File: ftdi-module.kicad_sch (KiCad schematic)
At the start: 56 parts, among them U1 USB4145-03-0070-c_REVA2, U2 ISO1641, U3 NCP163ASN330T1G, U5 FT4232H-56Q, Y1 KX-7_12,MHz

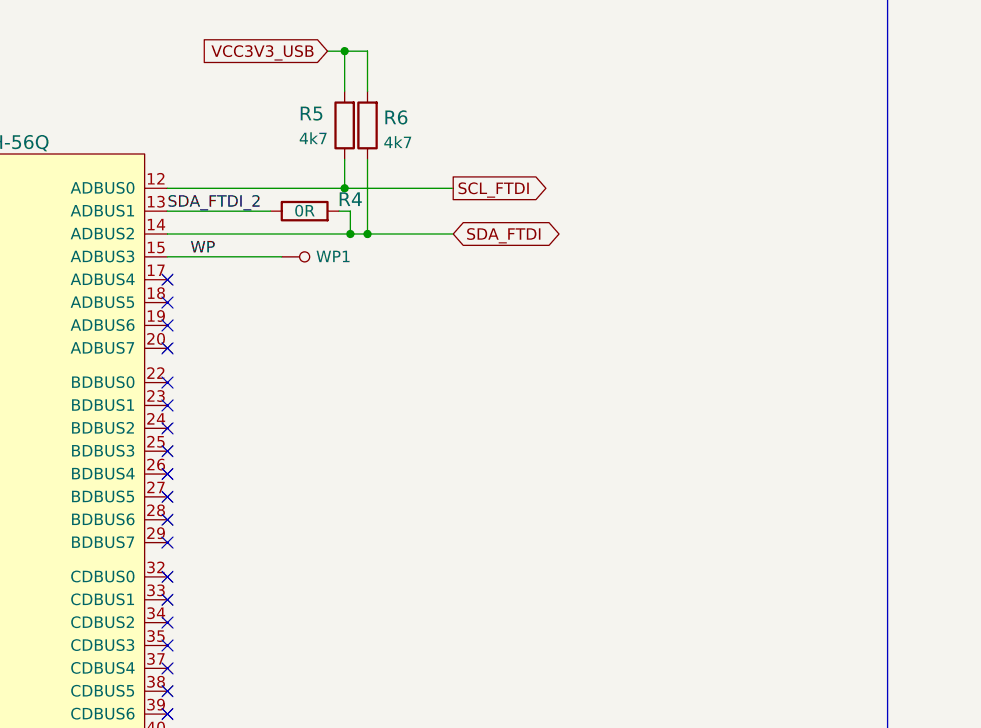
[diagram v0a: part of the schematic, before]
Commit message: #50436 Add FTDI led control, bump revision to 1.4.2
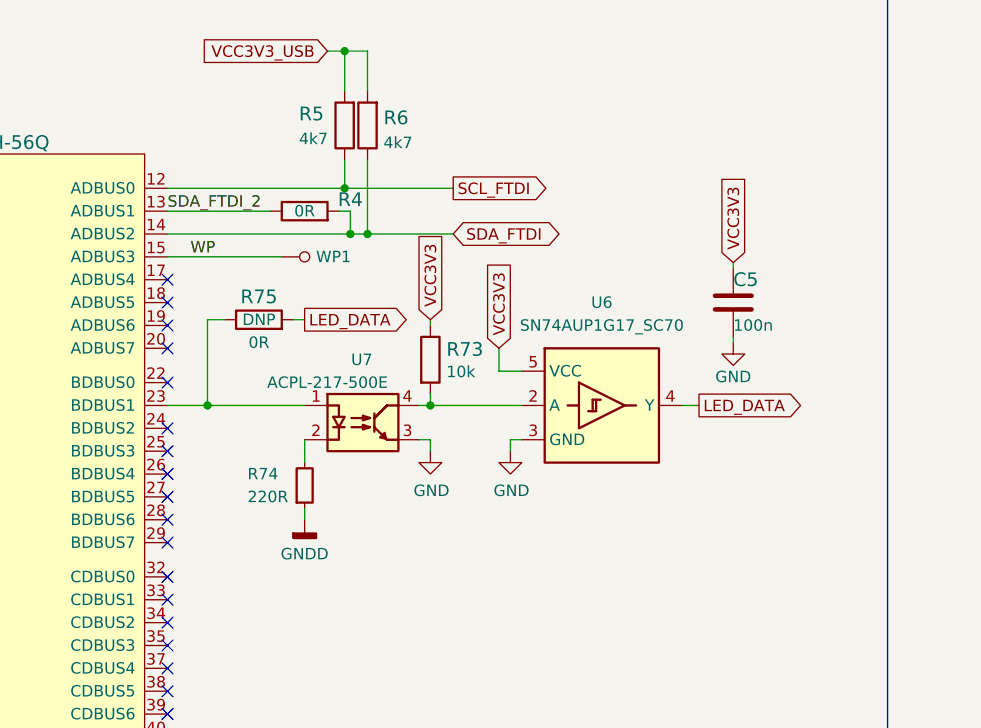
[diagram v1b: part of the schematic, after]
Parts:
- added C5: C_100n_0402, d1600e-psu-breakout-board-footprints:0402-cap, symbol d1600e-psu-breakout-board:C_100n_0402
- added R73: R_10k_0402, d1600e-psu-breakout-board-footprints:0402-res, symbol d1600e-psu-breakout-board:R_10k_0402
- added R74: R_220R_0402, antmicro-footprints:R_0402_1005Metric, symbol antmicroResistors0402:R_220R_0402
- added R75: R_0R_0603, d1600e-psu-breakout-board-footprints:0603-res, symbol d1600e-psu-breakout-board:R_0R_0603
- added U6: SN74AUP1G17_SC70, antmicro-footprints:SC-70-5, symbol antmicroLogicBuffersDriversReceiversTransceivers:SN74AUP1G17_SC70
- added U7: ACPL-217-500E, antmicro-footprints:SOIC-4_4.55x2.6mm_P1.27mm, symbol antmicroOptoisolatorsLogicOutput:ACPL-217-500E
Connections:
- net GND: now also C5.2, U6.3 (GND), U7.3
- net GNDD: now also R74.1
- net VCC3V3: now also C5.1, R73.1, U6.5 (VCC)
- net at U5.23 (BDBUS1): now also R75.1, U7.1
- new net: R73.2, U6.2 (A), U7.4
- new net: R74.2, U7.2
- new net LED_DATA: R75.2, U6.4 (Y)
- no-connect marks 33 -> 32

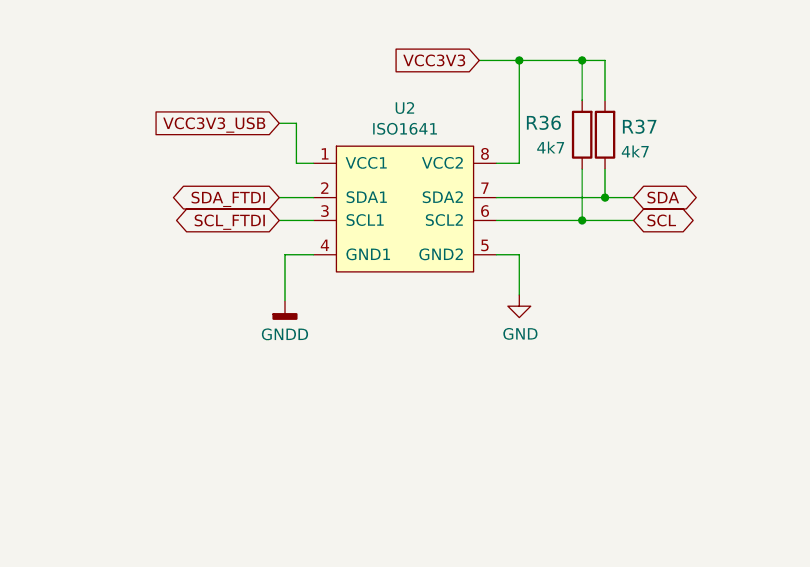
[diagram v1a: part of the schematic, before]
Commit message: #50436 Set U2 as DNP, add assembly variant table, bump to 1.4.3
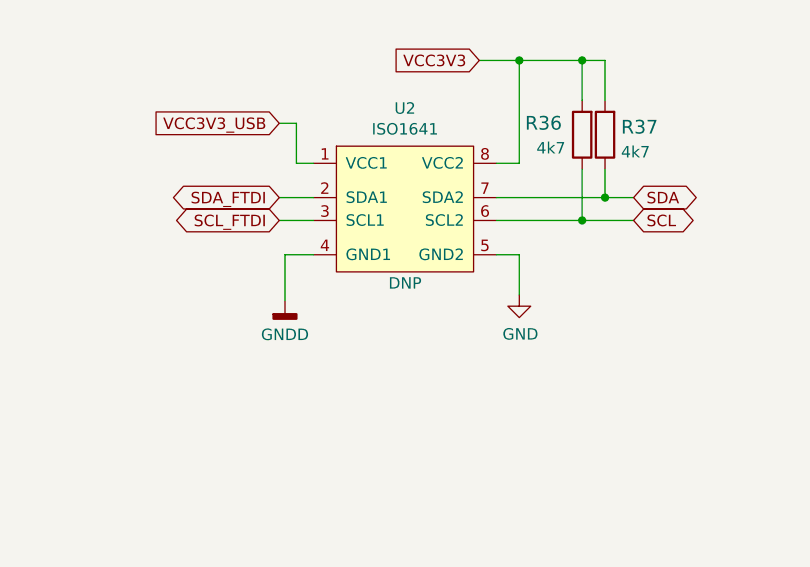
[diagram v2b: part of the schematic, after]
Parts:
- U2: DNP (none) -> DNP
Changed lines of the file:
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@@
     (title "D1600E PSU Breakout Board")
     (date "2023-10-18")
-    (rev "1.4.2")
+    (rev "1.4.3")
     (comment 1 "www.antmicro.com")
     (comment 2 "Antmicro Ltd.")
@@
       (effects (font (size 1.27 1.27)) hide)
     )
+    (property "DNP" "DNP" (id 6) (at 78.74 242.57 0))
     (pin "1")
     (pin "2")

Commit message: [#63472] Add OHP assets
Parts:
- removed TP1, TP2, TP3, TP4: TP_SMD1MM, antmicro-footprints:Testpoint_smd_1mm, symbol antmicroTestPoints:TP_SMD1MM
- added TP1, TP2, TP3, TP4: TP_1mm_SMD, antmicro-footprints:TP_SMD_1mm, symbol antmicroTestPoints:TP_1mm_SMD
- 3V3, 3V3_USB1, 5V_USB1, SCL1, SCL_FTDI1, SDA1, SDA_FTDI1, WP1: value TP_SMD1MM -> TP_1mm_SMD; footprint d1600e-psu-breakout-board-footprints:Testpoint_smd_1mm -> antmicro-footprints:TP_SMD_1mm; symbol d1600e-psu-breakout-board:TP_SMD1MM -> antmicroTestPoints:TP_1mm_SMD; Author (none) -> Antmicro; License (none) -> Apache-2.0; now left out of the parts list
- C1, C2: footprint antmicro-footprints:0402-cap -> antmicro-footprints:C_0402_1005Metric; Author (none) -> Antmicro; License (none) -> Apache-2.0; MPN MC0402N180J500CT -> CL05C180JB51PNC; Manufacturer MULTICOMP -> Samsung Electro-Mechanics
- C10, C14, C15, C16, C17, C18, C3, C4, C5, C6, C7, C8, C9: footprint d1600e-psu-breakout-board-footprints:0402-cap -> antmicro-footprints:C_0402_1005Metric; symbol d1600e-psu-breakout-board:C_100n_0402 -> antmicroCapacitors0402:C_100n_0402; Author (none) -> Antmicro; Dielectric (none) -> X5R; License (none) -> Apache-2.0; Voltage (none) -> 50V
- C11, C12, C13, C19, C20: footprint d1600e-psu-breakout-board-footprints:0402-cap -> antmicro-footprints:C_0402_1005Metric; symbol d1600e-psu-breakout-board:C_4u7_0402 -> antmicroCapacitors0402:C_4u7_0402; Author (none) -> Antmicro; License (none) -> Apache-2.0; Manufacturer MURATA -> Murata
- D1, D14: footprint d1600e-psu-breakout-board-footprints:TPD2E009DRTR -> antmicro-footprints:TPD2E009DRTR; symbol d1600e-psu-breakout-board:PESD5V0S2BQA -> antmicroTVSDiodes:PESD5V0S2BQA; Author (none) -> Antmicro; License (none) -> Apache-2.0
- D2: value LG_L29K-G2J1-24-Z -> LED_G_0603_LG_L29K-G2J1-24-Z; footprint d1600e-psu-breakout-board-footprints:LED_0603 -> antmicro-footprints:LED_0603_1608Metric_G; symbol d1600e-psu-breakout-board:LG_L29K-G2J1-24-Z -> antmicroLEDIndicationDiscrete:LED_G_0603_LG_L29K-G2J1-24-Z; Author (none) -> Antmicro; Color (none) -> Green; License (none) -> Apache-2.0; Manufacturer OSRAM Opto Semiconductors Inc. -> OSRAM
- FB1, FB2, FB3: value BLM18AG601SN1D -> FB_600Z_0.5A_Murata-BLM18AG_0603; footprint d1600e-psu-breakout-board-footprints:0603 -> antmicro-footprints:FB_0603_1608Metric; symbol d1600e-psu-breakout-board:BLM18AG601SN1D -> antmicroFerriteBeadsandChips:FB_600Z_0.5A_Murata-BLM18AG_0603; Author (none) -> Antmicro; License (none) -> Apache-2.0; Manufacturer Murata Electronics North America -> Murata; Val (none) -> 600Z/0.5A
- R1: footprint d1600e-psu-breakout-board-footprints:0402-res -> antmicro-footprints:R_0402_1005Metric; symbol d1600e-psu-breakout-board:R_1k_0402 -> antmicroResistors0402:R_1k_0402; Author (none) -> Antmicro; License (none) -> Apache-2.0; Manufacturer BOURNS -> Bourns; Tolerance (none) -> 1%
- R3: footprint d1600e-psu-breakout-board-footprints:0402-res -> antmicro-footprints:R_0402_1005Metric; symbol d1600e-psu-breakout-board:R_12k_0402 -> antmicroResistors0402:R_12k_0402; Author (none) -> Antmicro; License (none) -> Apache-2.0; MPN CRCW040212K0FKEDHP -> CR0402-FX-1202GLF; Manufacturer VISHAY -> Bourns; Tolerance (none) -> 1%
- R36, R37, R5, R6: footprint antmicro-footprints:0402-res -> antmicro-footprints:R_0402_1005Metric; Author (none) -> Antmicro; License (none) -> Apache-2.0; MPN MCS04020C4701FE000 -> CR0402-FX-4701GLF; Manufacturer VISHAY -> Bourns; Tolerance (none) -> 1%
- R38, R39, R42, R75: footprint d1600e-psu-breakout-board-footprints:0603-res -> antmicro-footprints:R_0603_1608Metric; symbol d1600e-psu-breakout-board:R_0R_0603 -> antmicroResistors0603:R_0R_0603; Author (none) -> Antmicro; Current (none) -> 1A; License (none) -> Apache-2.0; Manufacturer BOURNS -> Bourns; now not fitted; now left out of the parts list
- R4, R8: footprint d1600e-psu-breakout-board-footprints:0603-res -> antmicro-footprints:R_0603_1608Metric; symbol d1600e-psu-breakout-board:R_0R_0603 -> antmicroResistors0603:R_0R_0603; Author (none) -> Antmicro; Current (none) -> 1A; License (none) -> Apache-2.0; Manufacturer BOURNS -> Bourns
- R57, R58: footprint antmicro-footprints:0402-res -> antmicro-footprints:R_0402_1005Metric; Author (none) -> Antmicro; License (none) -> Apache-2.0; MPN SFR01MZPJ512 -> CR0402-FX-5101GLF; Manufacturer ROHM Semiconductor -> Bourns; Tolerance (none) -> 1%
- R7: footprint d1600e-psu-breakout-board-footprints:0402-res -> antmicro-footprints:R_0402_1005Metric; symbol d1600e-psu-breakout-board:R_330R_0402 -> antmicroResistors0402:R_330R_0402; Author (none) -> Antmicro; License (none) -> Apache-2.0; MPN MCMR04X3300FTL -> CR0402-FX-3300GLF; Manufacturer MULTICOMP -> Bourns; Tolerance (none) -> 1%
- R73: footprint d1600e-psu-breakout-board-footprints:0402-res -> antmicro-footprints:R_0402_1005Metric; symbol d1600e-psu-breakout-board:R_10k_0402 -> antmicroResistors0402:R_10k_0402; Author (none) -> Antmicro; License (none) -> Apache-2.0; MPN CRCW040210K0FKEDHP -> CR0402-FX-1002GLF; Manufacturer VISHAY -> Bourns; Tolerance (none) -> 1%
- U1: value USB4145-03-0070-c_REVA2 -> USB-C_GCT_USB4145-03-0070-C; footprint antmicro-footprints:GCT_USB4145-03-0070-C_REVA -> antmicro-footprints:USB-C_Receptacle_GCT_USB4145-03-0070-C; symbol antmicroUSBDVIHDMIConnectors:USB4145-03-0070-c_REVA -> antmicroUSBConnectors:USB-C_GCT_USB4145-03-0070-C; Author (none) -> Antmicro; License [SnapEDA CC BY-SA License](https://www.snapeda.com/about/te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 -> Apache-2.0
- U2: footprint d1600e-psu-breakout-board-footprints:SOIC-8_W3.9mm -> antmicro-footprints:SOIC-8_3.9x4.9x1.75mm_P1.27mm; symbol d1600e-psu-breakout-board:ISO1641 -> antmicroOptoisolatorsLogicOutput:ISO1641; Author (none) -> Antmicro; DNP DNP -> (none); License (none) -> Apache-2.0
- U3: footprint d1600e-psu-breakout-board-footprints:SOT-23-5 -> antmicro-footprints:SOT-23-5; symbol d1600e-psu-breakout-board:NCP163ASN330T1G -> antmicroPMICVoltageRegulatorsLinear:NCP163ASN330T1G; Author (none) -> Antmicro; License (none) -> Apache-2.0; Manufacturer Onsemi -> ON Semiconductor
- U5: value FT4232H-56Q -> FT4232H_VQFN; footprint d1600e-psu-breakout-board-footprints:QFN-56-1EP_8x8mm_P0.5mm_EP5.5.9x5.9mm -> antmicro-footprints:QFN-56-1EP_8x8mm_P0.5mm; symbol d1600e-psu-breakout-board:FT4232H-56Q -> antmicroInterfaceControllers:FT4232H_VQFN; Author (none) -> Antmicro; License (none) -> Apache-2.0; Manufacturer FTDI -> FTDI Chip
- Y1: value KX-7_12,MHz -> Resonator_12MHz_KX_7; footprint d1600e-psu-breakout-board-footprints:KX-7 -> antmicro-footprints:Resonator_SMD_Geyer_KX-7_3.2x2.5x0.8mm; symbol d1600e-psu-breakout-board:KX-7_12,MHz -> antmicroResonators:Resonator_12MHz_KX-7; Author (none) -> Antmicro; License (none) -> Apache-2.0; Val (none) -> 12 MHz
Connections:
- net 1V8_FT: now also C10.2, C13.2, C8.2, C9.2; no longer C10.1, C13.1, C8.1, C9.1
- net GND: now also C5.1; no longer C5.2
- net GNDD: now also C1.1, C10.1, C13.1, C16.1, C17.1, C19.1, C2.1, C20.1, C3.1, C4.1, C6.1, C7.1, C8.1, C9.1, D2.1 (C), U1.A1 (GND), U1.B1 (GND); no longer C1.2, C10.2, C13.2, C16.2, C17.2, C19.2, C2.2, C20.2, C3.2, C4.2, C6.2, C7.2, C8.2, C9.2, D2.2
- net OSCI: now also C2.2; no longer C2.1
- net OSCO: now also C1.2; no longer C1.1
- net VBUS: now also C17.2, U1.A4 (VBUS), U1.B4 (VBUS); no longer C17.1
- net VCC3V3: now also C5.2; no longer C5.1
- net VCC3V3_USB: now also C16.2, C20.2, C3.2, C4.2, C6.2, C7.2; no longer C16.1, C20.1, C3.1, C4.1, C6.1, C7.1
- net VCC5V0_USB: now also C19.2; no longer C19.1
- net at FB3.1: now also U1.SH; no longer U1.S2 (SHIELD)
- net at R7.2: now also D2.2 (A); no longer D2.1
- net at R57.2, U1.A5 (CC_{1}): now also TP1.1
- net at U1.A8 (SBU_{1}): now also TP2.1
- net at R58.1, U1.B5 (CC_{2}): now also TP4.1
- net at U1.B8 (SBU_{2}): now also TP3.1
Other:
- note removed: "Filtering"
- note removed: "Power Filtering"
- moved on the sheet: C1, C10, C11, C12, C13, C14, C15, C16, C17, C18, C19, C2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
